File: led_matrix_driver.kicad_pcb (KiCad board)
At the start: 4 copper layers, 59 parts, among them J1 Conn_01x03_Pin, J2 Screw_Terminal_01x02, J3 Screw_Terminal_01x02, J4 Conn_01x06_Pin, J5 Conn_02x17_Odd_Even, Q1 PXN020-100QSJ, Q2 TPH4R50ANH1,LQ, SW2 CK_KMS2xxGP, U1 LV5144RGYR, U2 Pico, U3 ESP32-WROOM-32, U4 AP1117-33, U6 Teensy4.0, U7 74AHCT541, U8 74AHCT541

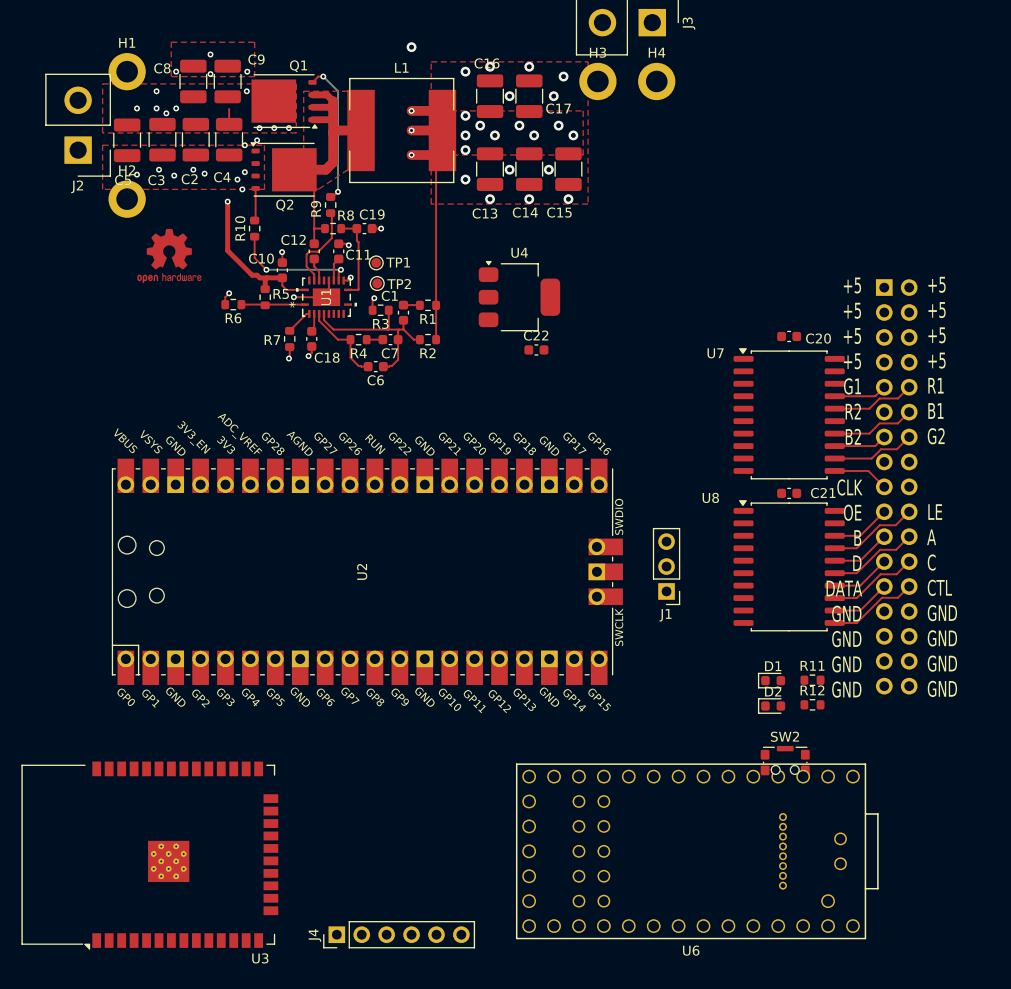
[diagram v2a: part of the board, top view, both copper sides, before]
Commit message: Routed data signals. Remove calibration data I2C wires
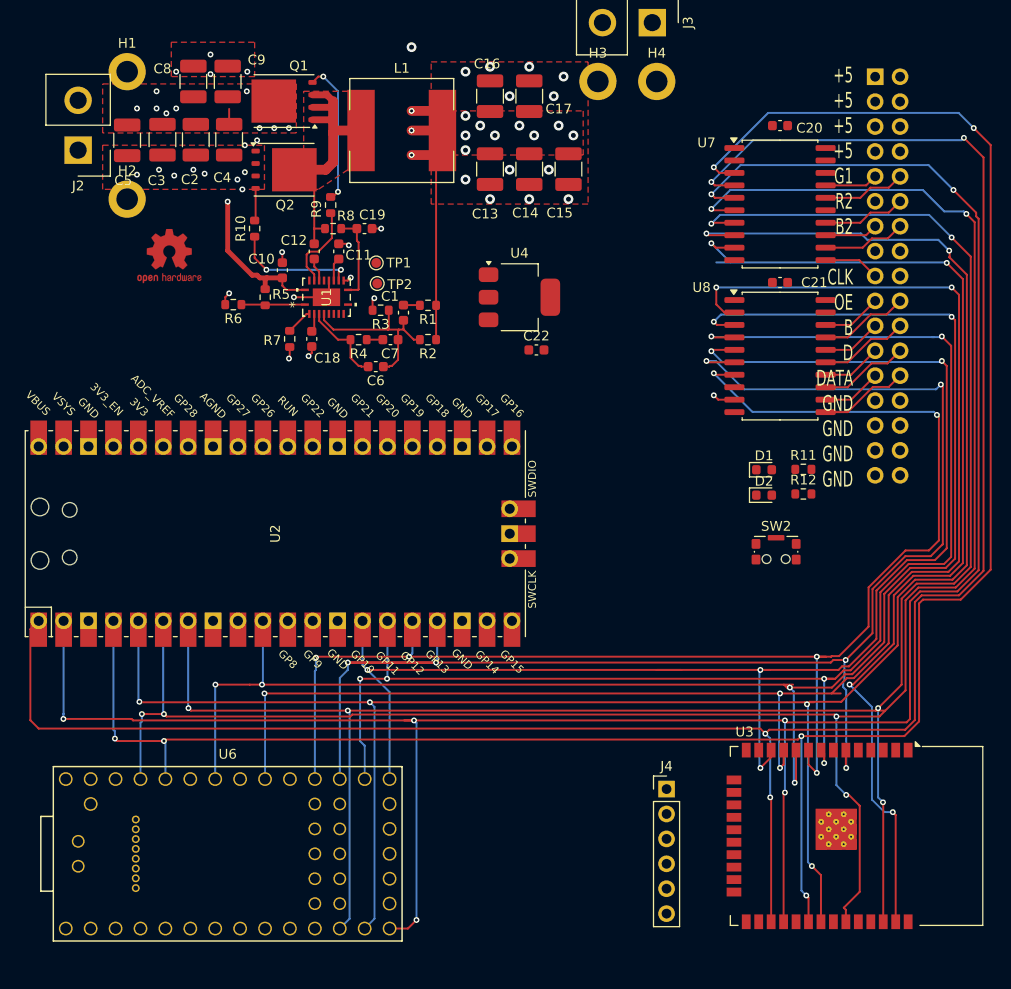
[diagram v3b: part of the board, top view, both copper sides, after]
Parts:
- removed J1: Conn_01x03_Pin, Connector_PinHeader_2.54mm:PinHeader_1x03_P2.54mm_Vertical
- moved U3 66.3 mm to (132.4, 136.9), turned to -90 degrees
- moved U6 47.3 mm to (71.2, 138.8), turned to 0 degrees
- moved J4 36.8 mm to (116.0, 132.2), turned to 0 degrees
- moved J5 21.5 mm to (137.3, 59.5)
- moved C20 21.5 mm to (127.6, 64.5)
- moved C21 21.5 mm to (127.6, 80.5)
- moved D1 21.5 mm to (125.9, 99.6)
- moved D2 21.5 mm to (125.9, 102.2)
- moved R11 21.5 mm to (129.9, 99.5)
- moved R12 21.5 mm to (129.9, 102.1)
- moved U7 21.5 mm to (127.6, 72.5)
- moved U8 21.5 mm to (127.6, 88.0)
- moved SW2 21.5 mm to (127.2, 108.0)
- moved U2 9.70 mm to (76.1, 106.1)
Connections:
- U2 pad 13: /A -> unconnected-(U2-GND-Pad13)
- U2 pad 14: /B -> /A
- U2 pad 15: /C -> /B
- U2 pad 16: /D -> /C
- U2 pad 17: unconnected-(U2-GPIO13-Pad17) -> /D
- U2 pad 41: Net-(J1-Pin_1) -> unconnected-(U2-SWCLK-Pad41)
- U2 pad 42: Net-(J1-Pin_2) -> unconnected-(U2-GND-Pad42)
- U2 pad 43: Net-(J1-Pin_3) -> unconnected-(U2-SWDIO-Pad43)_0
- U3 pad 10: unconnected-(U3-IO25-Pad10) -> /LE
- U3 pad 11: unconnected-(U3-IO26-Pad11) -> /OE
- U3 pad 12: unconnected-(U3-IO27-Pad12) -> /A
- U3 pad 27: unconnected-(U3-IO16-Pad27) -> /R1
- U3 pad 28: unconnected-(U3-IO17-Pad28) -> /R2
- U3 pad 30: unconnected-(U3-IO18-Pad30) -> /G1
- U3 pad 31: unconnected-(U3-IO19-Pad31) -> /G2
- U3 pad 33: unconnected-(U3-IO21-Pad33) -> /B1
- U3 pad 36: unconnected-(U3-IO22-Pad36) -> /B2
- U3 pad 37: unconnected-(U3-IO23-Pad37) -> /CLK
- U3 pad 6: unconnected-(U3-IO34-Pad6) -> /D
- U3 pad 8: unconnected-(U3-IO32-Pad8) -> /B
- U3 pad 9: unconnected-(U3-IO33-Pad9) -> /C
- U6 pad 1: unconnected-(U6-GND-Pad1) -> GND
- U6 pad 12: unconnected-(U6-10_CS_MQSR-Pad12) -> /B2
- U6 pad 13: unconnected-(U6-11_MOSI_CTX1-Pad13) -> /G2
- U6 pad 14: unconnected-(U6-12_MISO_MQSL-Pad14) -> /R2
- U6 pad 20: unconnected-(U6-13_SCK_CRX1_LED-Pad20) -> /A
- U6 pad 21: unconnected-(U6-14_A0_TX3_SPDIF_OUT-Pad21) -> /B
- U6 pad 22: unconnected-(U6-15_A1_RX3_SPDIF_IN-Pad22) -> /D
- U6 pad 23: unconnected-(U6-16_A2_RX4_SCL1-Pad23) -> /C
- U6 pad 25: unconnected-(U6-18_A4_SDA0-Pad25) -> /OE
- U6 pad 26: unconnected-(U6-19_A5_SCL0-Pad26) -> /CLK
- U6 pad 27: unconnected-(U6-20_A6_TX5_LRCLK1-Pad27) -> /LE
- U6 pad 28: unconnected-(U6-21_A7_RX5_BCLK1-Pad28) -> /R1
- U6 pad 29: unconnected-(U6-22_A8_CTX1-Pad29) -> /G1
- U6 pad 30: unconnected-(U6-23_A9_CRX1_MCLK1-Pad30) -> /B1
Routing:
- net /R2: track 0.00 -> 231.4 mm, vias 0 -> 7
- net /R1: track 0.00 -> 216.7 mm, vias 0 -> 4
- net /G1: track 0.00 -> 216.4 mm, vias 0 -> 6
- net /G2: track 0.00 -> 210.2 mm, vias 0 -> 6
- net /B2: track 0.00 -> 208.2 mm, vias 0 -> 6
- net /B1: track 0.00 -> 202.6 mm, vias 0 -> 6
- net /LE: track 0.00 -> 165.9 mm, vias 0 -> 6
- net /OE: track 0.00 -> 154.8 mm, vias 0 -> 5
- net /D: track 0.00 -> 151.3 mm, vias 0 -> 6
- net /A: track 0.00 -> 145.9 mm, vias 0 -> 5
- net /B: track 0.00 -> 144.7 mm, vias 0 -> 6
- net /C: track 0.00 -> 142.0 mm, vias 0 -> 6
- net /CLK: track 0.00 -> 106.3 mm, vias 0 -> 4
- net /CTL: track 0.00 -> 2.28 mm, vias 0 -> 1
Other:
- board text removed: "+5 +5 +5 +5 R1 B1 G2 LE A C CTL GND GND GND GND"

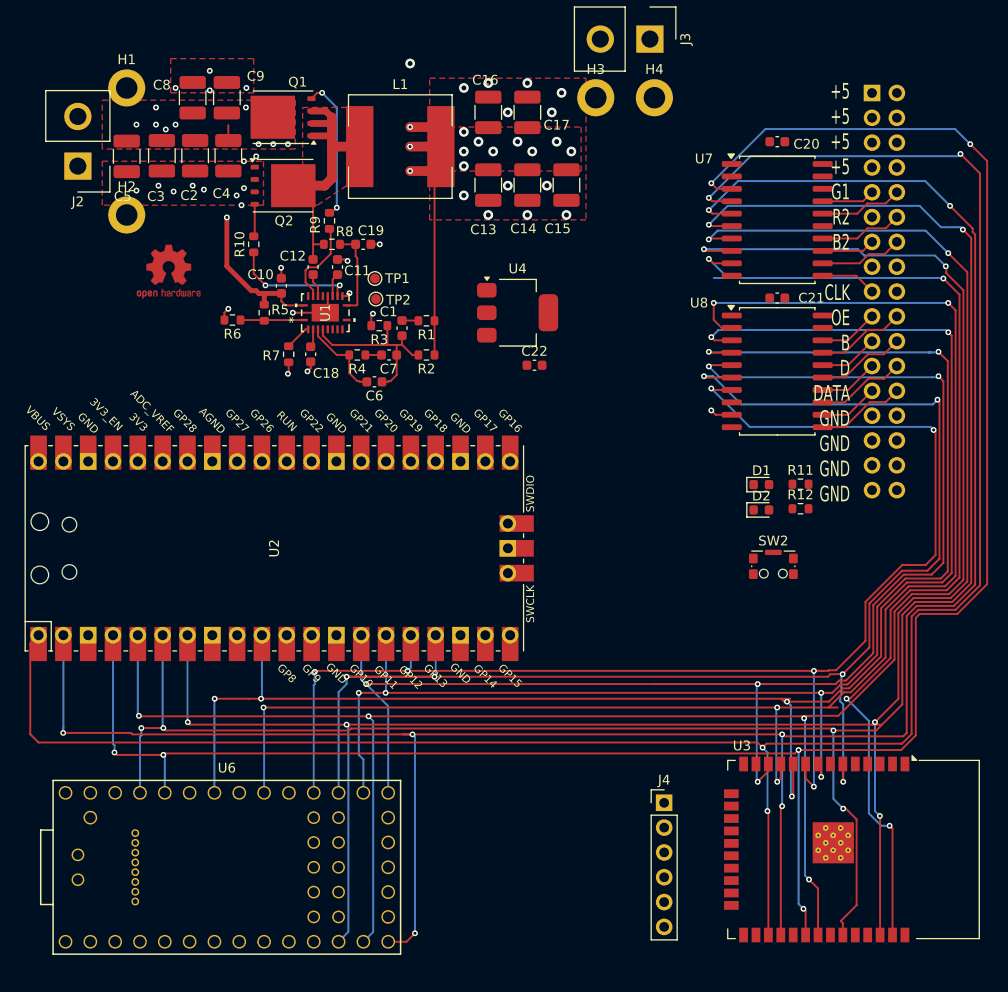
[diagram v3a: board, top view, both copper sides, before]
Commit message: Routed rest of the PCB
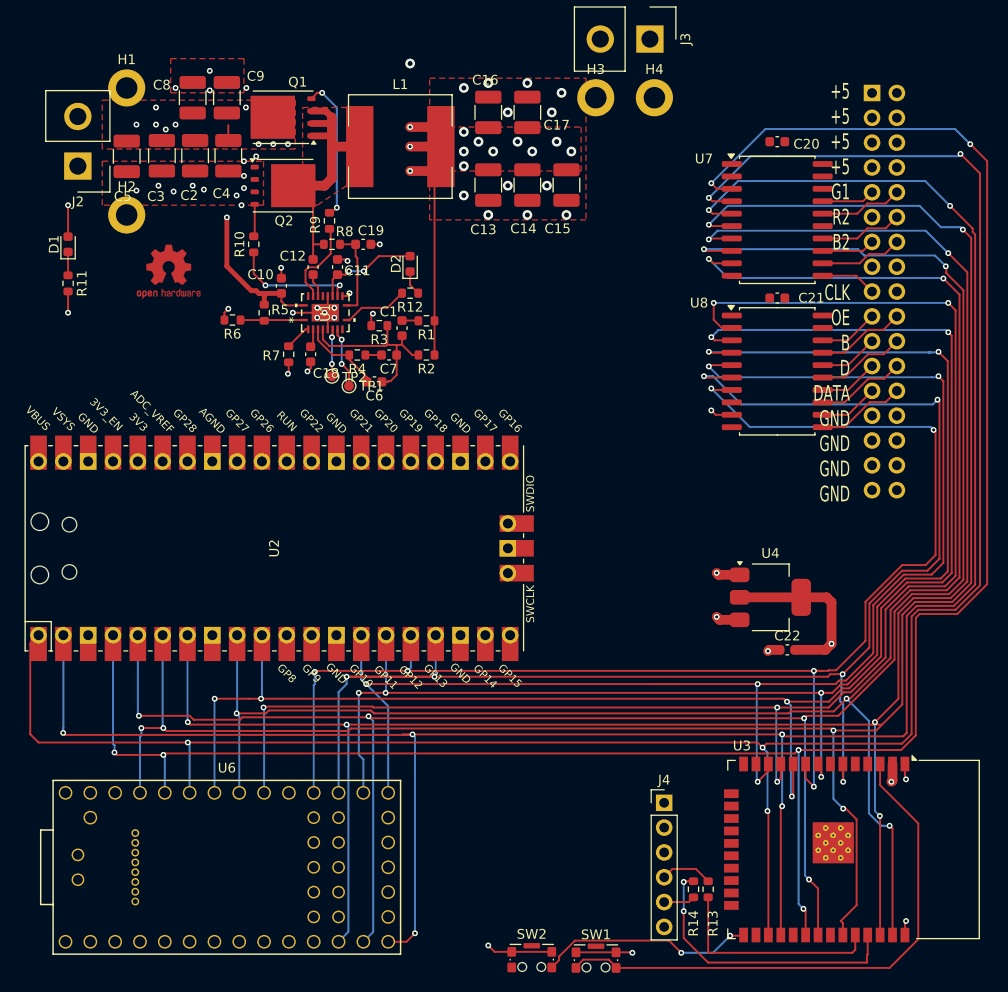
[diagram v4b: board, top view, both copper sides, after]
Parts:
- added R13: 0R, Resistor_SMD:R_0603_1608Metric, F.Cu at (120.5, 141.0)
- added R14: 0R, Resistor_SMD:R_0603_1608Metric, F.Cu at (119.0, 141.0)
- added SW1: CK_KMS2xxGP, Button_Switch_SMD:SW_SPST_CK_KMS2xxGP, F.Cu at (109.0, 148.2)
- moved R11 77.7 mm to (55.0, 79.0), turned to -90 degrees
- moved D1 75.1 mm to (55.0, 75.0), turned to 90 degrees
- moved SW2 47.2 mm to (102.5, 148.2)
- moved R12 45.6 mm to (90.0, 80.0), turned to 180 degrees
- moved D2 43.9 mm to (90.0, 77.0), turned to 90 degrees
- moved U4 39.0 mm to (126.9, 111.1)
- moved C22 39.0 mm to (128.6, 116.5)
- moved TP1 11.3 mm to (83.8, 89.5)
- moved TP2 9.09 mm to (82.0, 88.5)
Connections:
- J4 pad 1: unconnected-(J4-Pin_1-Pad1) -> GND
- J4 pad 4: unconnected-(J4-Pin_4-Pad4) -> Net-(J4-Pin_4)
- J4 pad 5: unconnected-(J4-Pin_5-Pad5) -> Net-(J4-Pin_5)
- SW2 pad 1: unconnected-(SW2-Pad1) -> GND
- SW2 pad 2: unconnected-(SW2-Pad2) -> Net-(U3-IO0)
- U3 pad 25: unconnected-(U3-IO0-Pad25) -> Net-(U3-IO0)
- U3 pad 3: unconnected-(U3-EN-Pad3) -> Net-(U3-EN)
- U3 pad 34: unconnected-(U3-RXD0/IO3-Pad34) -> Net-(U3-RXD0/IO3)
- U3 pad 35: unconnected-(U3-TXD0/IO1-Pad35) -> Net-(U3-TXD0/IO1)
- U7 pad 2: unconnected-(U7-A0-Pad2) -> GND
- U8 pad 8: /DATA -> unconnected-(U8-A6-Pad8)
- U8 pad 9: /CTL -> unconnected-(U8-A7-Pad9)
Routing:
- net /CLK: track 106.3 -> 184.5 mm, vias 4 -> 5
- net Net-(U3-EN): track 0.00 -> 56.6 mm
- net +3V3: track 0.00 -> 36.4 mm, vias 0 -> 2
- net Net-(U3-TXD0/IO1): track 0.00 -> 29.4 mm, vias 0 -> 2
- net GND: track 14.0 -> 37.3 mm, vias 36 -> 49
- net Net-(U3-RXD0/IO3): track 0.00 -> 22.4 mm
- net Net-(U3-IO0): track 0.00 -> 22.3 mm, vias 0 -> 2
- net /48 V to 5 V power supply/VCC: track 2.41 -> 10.6 mm, vias 0 -> 2
- net /48 V to 5 V power supply/POWER_GOOD: track 0.00 -> 6.79 mm
- net Net-(U1-SYNCIN): track 0.00 -> 6.28 mm, vias 0 -> 2
- net Net-(J4-Pin_4): track 0.00 -> 5.37 mm
- net /R1: track 216.7 -> 221.9 mm, vias 4 -> 5
- net Net-(U1-SYNCOUT): track 0.00 -> 4.83 mm, vias 0 -> 2
- net /48 V to 5 V power supply/48V_in: track 29.8 -> 33.0 mm, vias 10 -> 11
- net Net-(J4-Pin_5): track 0.00 -> 3.20 mm
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
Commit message: DRC fixes
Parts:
- moved J2 1.00 mm to (55.0, 67.0)
- moved SW1 0.55 mm to (109.0, 147.7)
- moved SW2 0.55 mm to (102.5, 147.7)
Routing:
- net /B2: track 208.2 -> 223.3 mm
- net Net-(U3-TXD0/IO1): track 29.4 -> 28.6 mm
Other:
- board outline added: 100 x 100 mm
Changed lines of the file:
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@@
 			(pinfunction "2")
 			(pintype "passive")
+			(zone_connect 2)
 		)
 		(model "${KICAD8_3DMODEL_DIR}/Inductor_SMD.3dshapes/L_10.4x10.4_H4.8.wrl"
@@
 	(footprint "Button_Switch_SMD:SW_SPST_CK_KMS2xxGP"
 		(layer "F.Cu")
-		(at 109.025 148.25)
+		(at 109.025 147.7)
 		(descr "Microminiature SMT Side Actuated, 4.2 x 2.8 x 1.42mm with pegs, https://www.ckswitches.com/media/1482/kms.pdf")
 		(tags "Switch SPST KMS2")
@@
 	(footprint "Connector_Samtec_HPM_THT:Samtec_HPM-02-01-x-S_Straight_1x02_Pitch5.08mm"
 		(layer "F.Cu")
-		(at 56 67 180)
+		(at 55 67 180)
 		(descr "Through hole straight Samtec HPM power header series 11.94mm post length, 1x02, 5.08mm pitch, single row")
 		(tags "Through hole Samtec HPM power header series 11.94mm post length THT 1x02 5.08mm single row")
@@
 	(footprint "Button_Switch_SMD:SW_SPST_CK_KMS2xxGP"
 		(layer "F.Cu")
-		(at 102.45 148.2)
+		(at 102.45 147.65)
 		(descr "Microminiature SMT Side Actuated, 4.2 x 2.8 x 1.42mm with pegs, https://www.ckswitches.com/media/1482/kms.pdf")
 		(tags "Switch SPST KMS2")
@@
 			(type default)
 		)
-		(layer "Margin")
+		(layer "Edge.Cuts")
 	)
 	(gr_line
@@
 			(type default)
 		)
-		(layer "Margin")
+		(layer "Edge.Cuts")
 	)
 	(gr_line
@@
 			(type default)
 		)
-		(layer "Margin")
+		(layer "Edge.Cuts")
 	)
 	(gr_line
@@
 			(type default)
 		)
-		(layer "Margin")
+		(layer "Edge.Cuts")
 	)
 	(gr_text "+5\n+5\n+5\n+5\nG1\nR2\nB2\n\nCLK\nOE\nB\nD\nDATA\nGND\nGND\nGND\nGND"
@@
 	)
 	(segment
-		(start 106.975 147.45)
-		(end 111.075 147.45)
+		(start 106.975 146.9)
+		(end 111.075 146.9)
 		(width 0.2)
 		(layer "F.Cu")
@@
 	)
 	(segment
-		(start 104.5 147.4)
-		(end 100.4 147.4)
+		(start 104.5 146.85)
+		(end 100.4 146.85)
 		(width 0.2)
 		(layer "F.Cu")
@@
 	)
 	(segment
-		(start 98.65 147.4)
-		(end 98 146.75)
+		(start 98.65 146.85)
+		(end 98 146.2)
 		(width 0.2)
 		(layer "F.Cu")
@@
 	)
 	(segment
-		(start 100.4 147.4)
-		(end 98.65 147.4)
+		(start 100.4 146.85)
+		(end 98.65 146.85)
 		(width 0.2)
 		(layer "F.Cu")
@@
 	)
 	(via
-		(at 98 146.75)
+		(at 98 146.2)
 		(size 0.6)
 		(drill 0.3)
@@
 	)
 	(segment
-		(start 118.075 140.175)
-		(end 118 140.25)
+		(start 136.4 148.1)
+		(end 120.1 148.1)
 		(width 0.2)
 		(layer "F.Cu")
@@
 	)
 	(segment
-		(start 120.5 148.5)
-		(end 118 146)
+		(start 118.075 140.175)
+		(end 118 140.25)
 		(width 0.2)
 		(layer "F.Cu")
@@
 	)
 	(segment
-		(start 136.75 147.75)
-		(end 136.825 147.675)
+		(start 136.825 147.675)
+		(end 136.4 148.1)
 		(width 0.2)
 		(layer "F.Cu")
@@
 	)
 	(segment
-		(start 136.825 147.675)
-		(end 136.825 145.68)
-		(width 0.2)
-		(layer "F.Cu")
-		(net 55)
-	)
-	(segment
-		(start 136.75 148.5)
-		(end 136.75 147.75)
+		(start 136.825 145.68)
+		(end 136.825 147.675)
 		(width 0.2)
 		(layer "F.Cu")
@@
 	)
 	(segment
-		(start 136.75 148.5)
-		(end 120.5 148.5)
+		(start 120.1 148.1)
+		(end 118 146)
 		(width 0.2)
 		(layer "F.Cu")
@@
 	)
 	(segment
-		(start 106.975 149.05)
-		(end 106.975 148.943629)
+		(start 106.975 148.5)
+		(end 106.975 148.393629)
 		(width 0.2)
 		(layer "F.Cu")
@@
 	)
 	(segment
-		(start 111.075 148.943629)
-		(end 111.075 149.05)
+		(start 111.075 148.393629)
+		(end 111.075 148.5)
 		(width 0.2)
 		(layer "F.Cu")
@@
 	)
 	(segment
-		(start 106.975 148.943629)
-		(end 107.718629 148.2)
+		(start 139.615 148.5)
+		(end 111.075 148.5)
 		(width 0.2)
 		(layer "F.Cu")
@@
 	)
 	(segment
-		(start 107.718629 148.2)
-		(end 110.331371 148.2)
+		(start 106.975 148.393629)
+		(end 107.718629 147.65)
 		(width 0.2)
 		(layer "F.Cu")
@@
 	)
 	(segment
-		(start 111.075 149.05)
-		(end 139.065 149.05)
+		(start 142 146.115)
+		(end 139.615 148.5)
 		(width 0.2)
 		(layer "F.Cu")
@@
 	)
 	(segment
-		(start 110.331371 148.2)
-		(end 111.075 148.943629)
+		(start 107.718629 147.65)
+		(end 110.331371 147.65)
 		(width 0.2)
 		(layer "F.Cu")
@@
 	)
 	(segment
-		(start 142 146.115)
-		(end 142 134.25)
+		(start 110.331371 147.65)
+		(end 111.075 148.393629)
 		(width 0.2)
 		(layer "F.Cu")
@@
 	)
 	(segment
-		(start 138.095 130.345)
-		(end 138.095 128.18)
+		(start 142 146.115)
+		(end 142 134.25)
 		(width 0.2)
 		(layer "F.Cu")
@@
 	)
 	(segment
-		(start 139.065 149.05)
-		(end 142 146.115)
+		(start 138.095 130.345)
+		(end 138.095 128.18)
 		(width 0.2)
 		(layer "F.Cu")
@@
 	)
 	(segment
-		(start 54.52 124.48)
-		(end 54.52 115)
+		(start 128.47 132.1)
+		(end 128.07 132.5)
 		(width 0.2)
 		(layer "B.Cu")
@@
 	)
 	(segment
-		(start 90.5 145.5)
-		(end 90.5 125.4)
+		(start 128.47 125.55)
+		(end 128.47 132.1)
 		(width 0.2)
 		(layer "B.Cu")
@@
 	)
 	(segment
-		(start 128.07 132.5)
-		(end 128.07 125.15)
+		(start 54.52 124.48)
+		(end 54.52 115)
+		(width 0.2)
+		(layer "B.Cu")
+		(net 90)
+	)
+	(segment
+		(start 90.5 145.5)
+		(end 90.5 125.4)
 		(width 0.2)
 		(layer "B.Cu")
@@
 	)
 	(segment
+		(start 128.07 125.15)
+		(end 128.47 125.55)
+		(width 0.2)
+		(layer "B.Cu")
+		(net 90)
+	)
+	(segment
 		(start 54.5 124.5)
 		(end 54.52 124.48)
@@
 	)
 	(segment
-		(start 139.97 121.5)
-		(end 139.97 112.740835)
+		(start 137.57 123.9)
+		(end 137.32 124.15)
 		(width 0.2)
 		(layer "F.Cu")
@@
 	)
 	(segment
-		(start 122.92 74.405)
-		(end 120.665 74.405)
+		(start 139.97 121.5)
+		(end 139.97 112.740835)
 		(width 0.2)
 		(layer "F.Cu")
@@
 	)
 	(segment
-		(start 138.25 124.15)
-		(end 83.5 124.15)
+		(start 122.92 74.405)
+		(end 120.665 74.405)
 		(width 0.2)
 		(layer "F.Cu")
@@
 	)
 	(segment
-		(start 138.07 133.5)
-		(end 138.095 133.525)
+		(start 137.32 124.15)
+		(end 67.5 124.15)
 		(width 0.2)
 		(layer "F.Cu")
@@
 	)
 	(segment
-		(start 137.57 123.9)
-		(end 137.32 124.15)
+		(start 138.07 133.5)
+		(end 138.095 133.525)
 		(width 0.2)
 		(layer "F.Cu")
@@
 	)
 	(segment
-		(start 105.25 147.876076)
-		(end 106.876076 146.25)
+		(start 105.25 147.326076)
+		(end 106.876076 145.7)
 		(width 0.2)
 		(layer "F.Cu")
@@
 	)
 	(segment
-		(start 104.5 149)
-		(end 105.25 148.25)
+		(start 104.5 148.45)
+		(end 105.25 147.7)
 		(width 0.2)
 		(layer "F.Cu")
@@
 	)
 	(segment
-		(start 106.876076 146.25)
-		(end 116.5 146.25)
+		(start 106.876076 145.7)
+		(end 115.223654 145.7)
 		(width 0.2)
 		(layer "F.Cu")
@@
 	)
 	(segment
-		(start 105.25 148.25)
-		(end 105.25 147.876076)
+		(start 105.25 147.7)
+		(end 105.25 147.326076)
 		(width 0.2)
 		(layer "F.Cu")
@@
 		(width 0.2)
 		(layer "F.Cu")
+		(net 105)
+	)
+	(segment
+		(start 115.773654 146.25)
+		(end 116.5 146.25)
+		(width 0.2)
+		(layer "F.Cu")
+		(net 105)
+	)
+	(segment
+		(start 115.223654 145.7)
+		(end 115.773654 146.25)
+		(width 0.2)
+		(layer "F.Cu")

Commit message: DRC fixes
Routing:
- net GND: track 37.3 -> 56.8 mm, vias 49 -> 59
- net +5V: track 37.8 -> 52.3 mm, vias 13 -> 15
- net /LED_DR2: track 0.00 -> 5.43 mm
- net Net-(U3-IO0): track 22.5 -> 27.8 mm
- net /48 V to 5 V power supply/SW: track 29.6 -> 34.4 mm
- net unconnected-(U8-A7-Pad9): track 2.28 -> 0.00 mm, vias 1 -> 0
